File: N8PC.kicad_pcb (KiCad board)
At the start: 4 copper layers, 244 x 244 mm, 226 parts, among them J1 IRQ Selection, J10 Bus_ISA_8bit, J11 F18A TANG NANO Connector, J12 FRONT_PANEL, J13 IRQ Selection, J14 Bus_ISA_8bit, J15 MOUSE, J16 KEYBOARD, J17 TTL SERIAL CONSOLE, J18 TTL CONSOLE PWR, J19 TTL SERIAL CONSOLE, J2 IRQ Selection, J20 TTL CONSOLE PWR, J21 KEYBOARD IRQ, J22 BUS IRQ, J23 VIDEO IRQ, J3 Bus_ISA_8bit, J4 Bus_ISA_8bit, J5 IRQ Selection, J6 Bus_ISA_8bit, J7 IRQ Selection, J8 Bus_ISA_8bit, J9 IRQ Selection, K16 CONN_3, K17 CPU_CLK, K18 CONN_3, K2 IDE_PWR, K3 CONN_3, K4 CONN_3, K5 CONN_3, P1 IO_ADDR, P10 CONN_1, P11 CONN_10X2, P12 POWER_SW, P13 SERIAL, P14 14.31818 MHz CLK, P15 AUDIO, P16 IO_ADDR2, P18 SERIAL, P19 ASCI OSC, P2 CONN_1, P21 CONN_1, P22 CONN_1, P23 CONN_1, P27 FLOPPY, P29 PPIDE, P3 CONN_1, P31 PARALLEL EXP, P37 CPU OSC, P4 CONN_1, P41 OSC_FDC, P43 CHAN_MIX, P5 CONN_1, P51 JOYSTICK0, P52 JOYSTICK1, P6 CONN_1, P7 CONN_1, P8 CONN_1, P9 CONN_1, SW1 POWER, SW2 RESET, U1 74LS244, U10 MAX232, U12 74LS74, U13 27C080, U14 74LS125, U15 74LS245, U16 74LS244, U18 74LS32, U19 74HCT14, U2 74LS14, U21 74LS682N, U23 TMS9918 EMU, U24 CLK, U25 82c42, U26 74LS06, U29 DS1233, U3 74LS244, U31 74LS244, U32 74LS139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

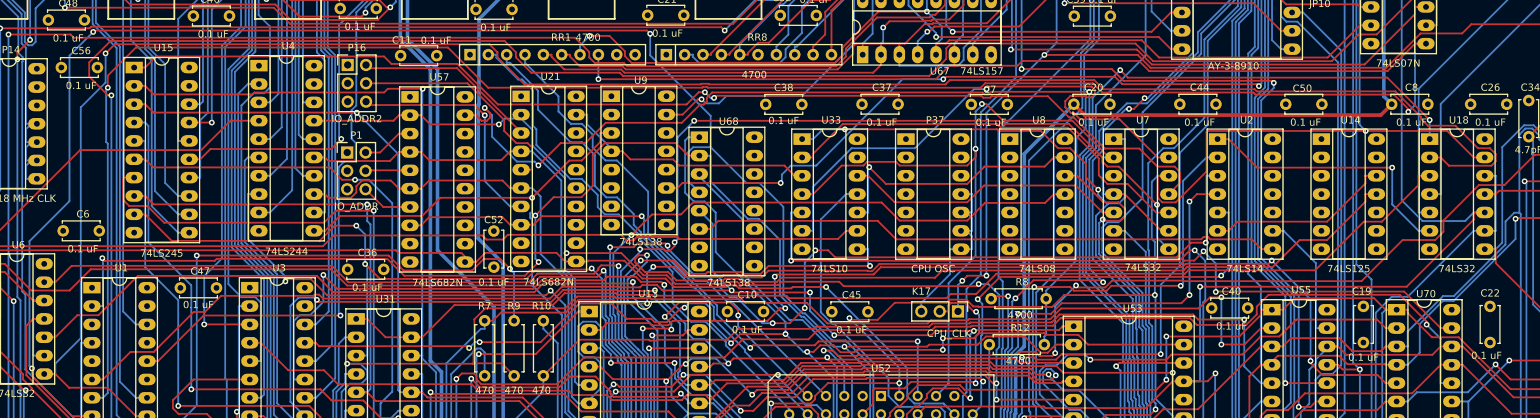
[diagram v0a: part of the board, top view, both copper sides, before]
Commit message: update for front panel fix
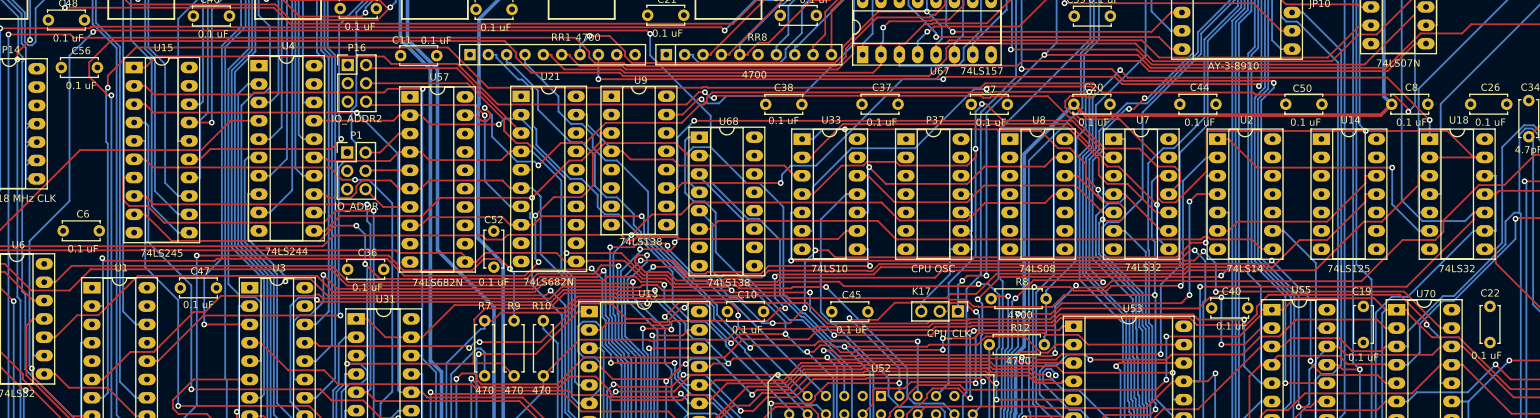
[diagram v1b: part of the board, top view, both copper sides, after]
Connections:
- U18 pad 2: Net-(U1-I1b) -> /RD
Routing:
- net Net-(U1-I1b): track 276.7 -> 16.6 mm, vias 1 -> 0
- net /RD: track 525.1 -> 532.7 mm
